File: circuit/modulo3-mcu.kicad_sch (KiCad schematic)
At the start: 24 parts, among them SW1 RST_SW, U1 74LVC2G32DC, U2 AVR64DA64, U3 SN74LVC1G17, U4 UPDI, Y1 32768Hz

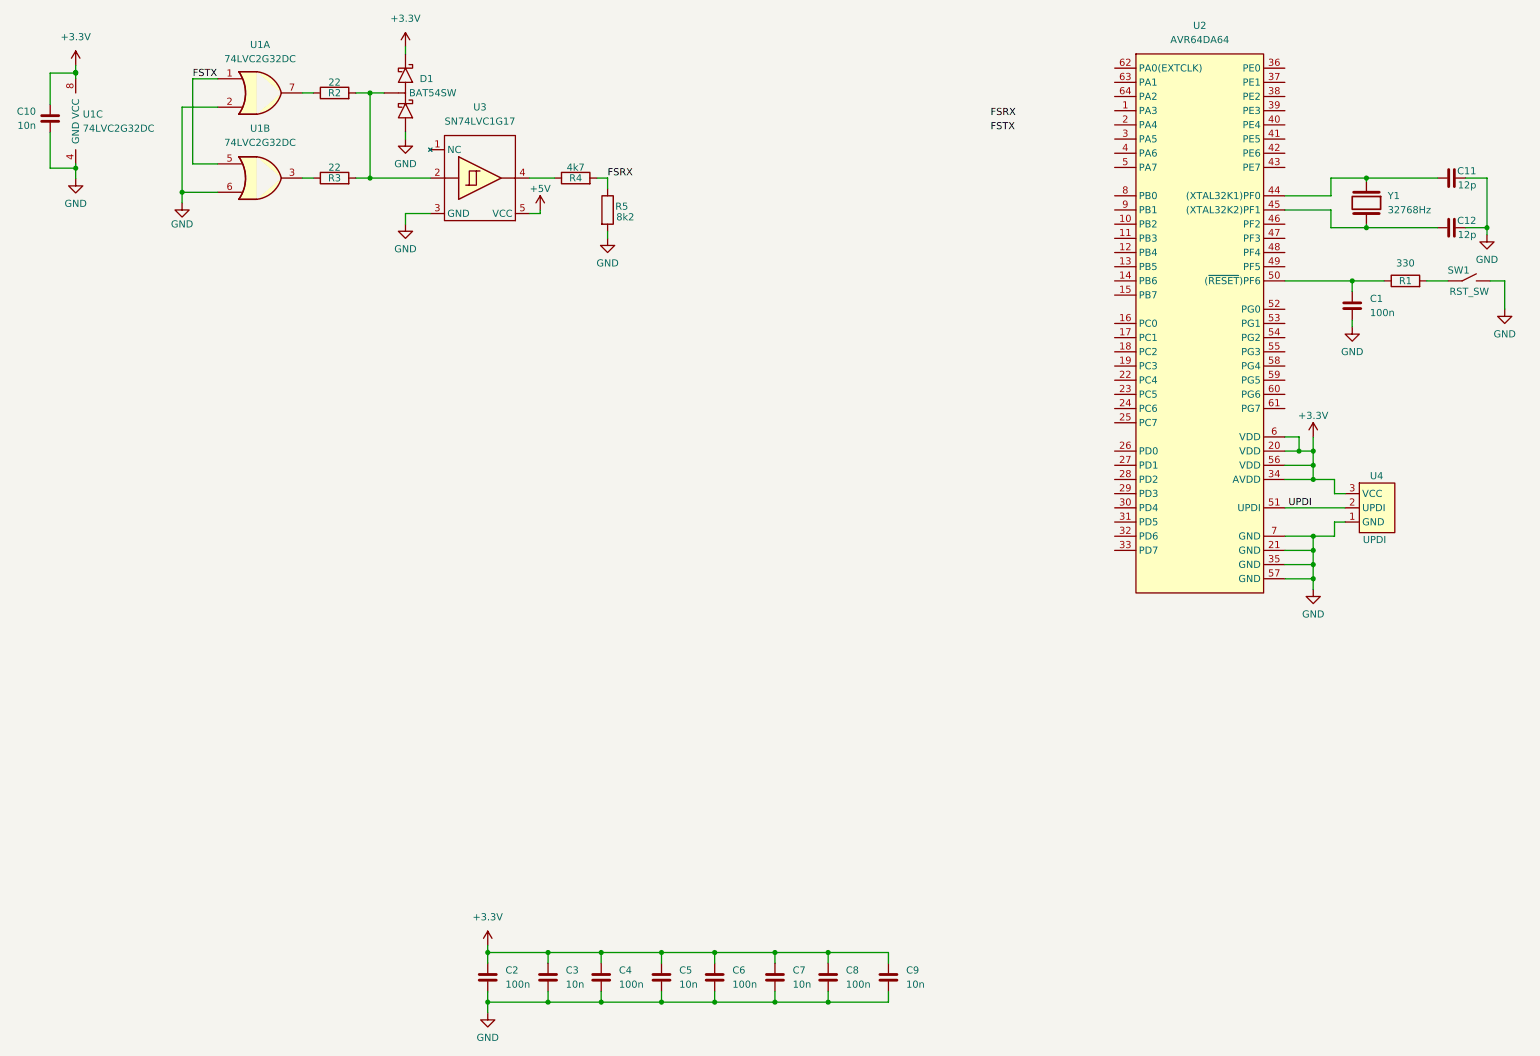
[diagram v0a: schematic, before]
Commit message: mcu board; fv1 board tracing
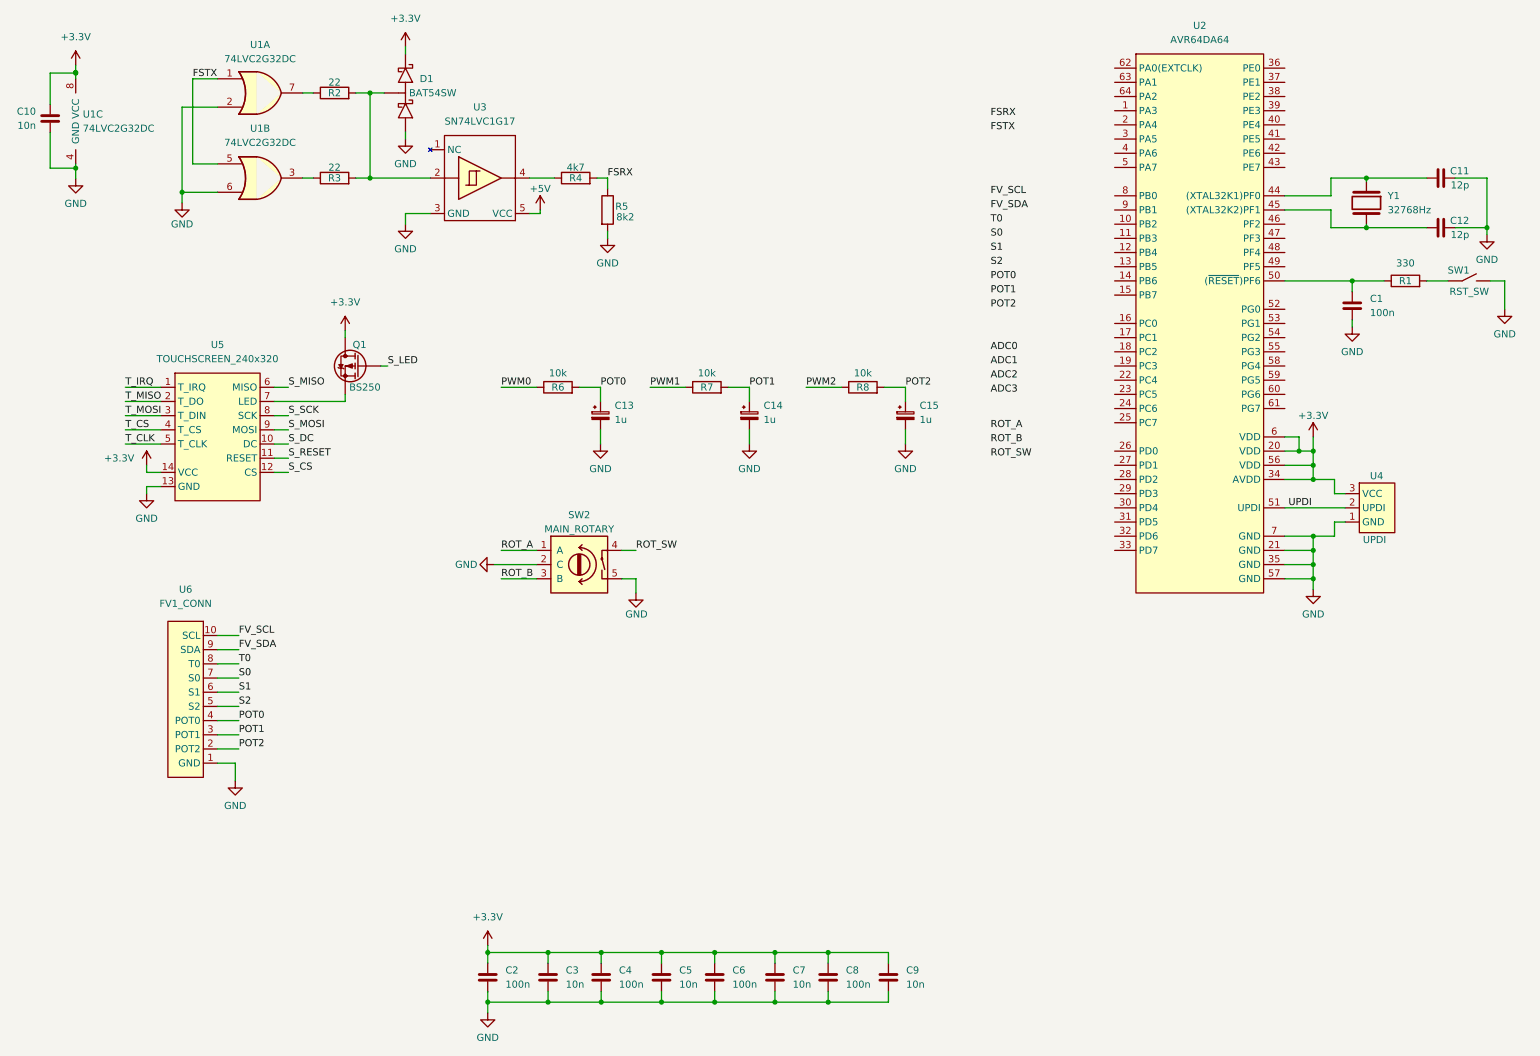
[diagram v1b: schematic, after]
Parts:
- added C13, C14, C15: 1u, symbol myAmp:CPOL
- added Q1: BS250, myAmp:TO-92_Inline_Wide, symbol myAmp:BS250
- added R6, R7, R8: 10k, myAmp:C_1206, symbol myAmp:R
- added SW2: MAIN_ROTARY, symbol myAmp:Rotary_Encoder_Switch
- added U5: TOUCHSCREEN_240x320, symbol myAmp:TOUCHSCREEN_240x320
- added U6: FV1_CONN, symbol myAmp:FV1_CONN
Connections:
- net +3.3V: now also Q1.1 (D), U5.14 (VCC)
- net GND: now also C13.2, C14.2, C15.2, SW2.2 (C), SW2.5, U5.13 (GND), U6.1 (GND)
- new net: Q1.3 (S), U5.7 (LED)
- new net FV_SCL: U6.10 (SCL)
- new net FV_SDA: U6.9 (SDA)
- new net POT0: C13.1, R6.2, U6.4 (POT0)
- new net POT1: C14.1, R7.2, U6.3 (POT1)
- new net POT2: C15.1, R8.2, U6.2 (POT2)
- new net PWM0: R6.1
- new net PWM1: R7.1
- new net PWM2: R8.1
- new net ROT_A: SW2.1 (A)
- new net ROT_B: SW2.3 (B)
- new net ROT_SW: SW2.4
- new net S0: U6.7 (S0)
- new net S1: U6.6 (S1)
- new net S2: U6.5 (S2)
- new net S_CS: U5.12 (CS)
- new net S_DC: U5.10 (DC)
- new net S_LED: Q1.2 (G)
- new net S_MISO: U5.6 (MISO)
- new net S_MOSI: U5.9 (MOSI)
- new net S_RESET: U5.11 (RESET)
- new net S_SCK: U5.8 (SCK)
- new net T0: U6.8 (T0)
- new net T_CLK: U5.5 (T_CLK)
- new net T_CS: U5.4 (T_CS)
- new net T_IRQ: U5.1 (T_IRQ)
- new net T_MISO: U5.2 (T_DO)
- new net T_MOSI: U5.3 (T_DIN)
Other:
- moved on the sheet: C11, C12

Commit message: added touchscreen footprint
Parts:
- added R9: 100, myAmp:C_1206, symbol myAmp:R
- C13, C14, C15: value 1u -> 3u3; footprint (none) -> myAmp:CPOL_D4_P1.5
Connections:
- net T_MISO is gone; now on net S_MISO: U5.2 (T_DO)
- net T_MOSI is gone; now on net S_MOSI: U5.3 (T_DIN)
- net at U5.7 (LED): now also R9.1; no longer Q1.3 (S)
- net T_CLK renamed S_CLK
- new net: Q1.3 (S), R9.2
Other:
- moved on the sheet: U5

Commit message: general layout and board sizes
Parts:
- removed C1: 100n, myAmp:C_1206, symbol myAmp:C
- removed R1: 330, myAmp:C_1206, symbol myAmp:R
- removed SW1: RST_SW, myAmp:Switch_2.5mm, symbol myAmp:SW_SIMPLE
- removed SW2: MAIN_ROTARY, symbol myAmp:Rotary_Encoder_Switch
- added U7: DBG_UART, myAmp:DBG_UART, symbol myAmp:DBG_UART
- R2, R3, R4, R5, R9: footprint myAmp:C_1206 -> myAmp:R_10MM
- R6, R7, R8: footprint myAmp:C_1206 -> myAmp:R_1206
- U5: footprint (none) -> myAmp:TOUCHSCREEN_2.8
- U6: footprint (none) -> myAmp:FV1_CONN
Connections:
- net S_CLK is gone; now on net S_SCK: U5.5 (T_CLK)
- net S_RESET is gone; now on net S_RST: U5.11 (RESET)
- net GND: now also U7.1 (GND)
- net PWM0: now also U2.62 (PA0(EXTCLK))
- net PWM1: now also U2.63 (PA1)
- net PWM2: now also U2.64 (PA2)
- net S_CS: now also U2.10 (PB2)
- net S_DC: now also U2.8 (PB0)
- net S_LED: now also U2.11 (PB3)
- net S_MISO: now also U2.3 (PA5)
- net S_MOSI: now also U2.2 (PA4)
- net S_SCK: now also U2.4 (PA6)
- net T_CS: now also U2.5 (PA7)
- net T_IRQ: now also U2.1 (PA3)
- net DBG_TX: now reaches U2.52 (PG0)
- net DBG_TX: now also U7.2 (TX)
- net S_RST: now reaches U2.9 (PB1)
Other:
- moved on the sheet: C10, C11, C12, U1C, U2, U4, Y1

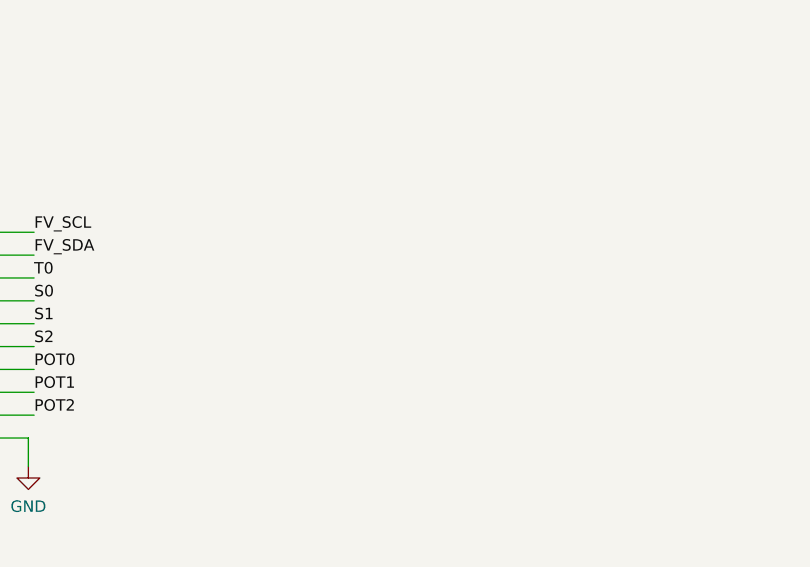
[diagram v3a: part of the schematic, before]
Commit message: added ampctrl and diffaudio; started changing powamp
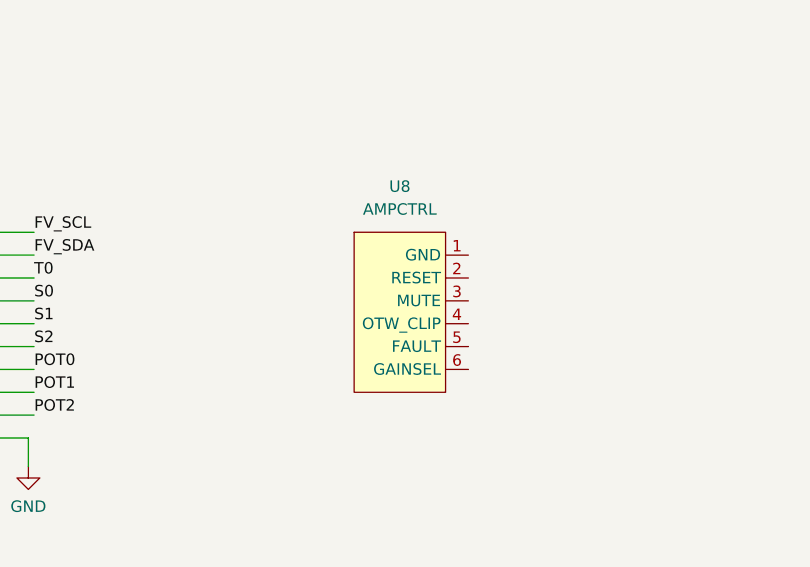
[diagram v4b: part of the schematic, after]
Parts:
- added U8: AMPCTRL, myAmp:AMPCTRL, symbol myAmp:AMPCTRL
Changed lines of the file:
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@@
     (pin "2")
+  )
+  (symbol (lib_id "myAmp:AMPCTRL") (at 95.25 129.54 0) (unit 1)
+    (in_bom yes) (on_board yes) (fields_autoplaced)
+    (property "Reference" "U8" (id 0) (at 93.98 119.38 0))
+    (property "Value" "AMPCTRL" (id 1) (at 93.98 121.92 0))
+    (property "Footprint" "myAmp:AMPCTRL" (id 2) (at 101.6 129.54 0)
+      (effects (font (size 1.27 1.27)) hide)
+    )
+    (property "Datasheet" "" (id 3) (at 101.6 129.54 0))
+    (pin "1")
+    (pin "2")
+    (pin "3")
+    (pin "4")
+    (pin "5")
+    (pin "6")
   )
   (symbol (lib_id "myAmp:C") (at 158.877 185.674 0) (unit 1)
@@
       (reference "U7") (unit 1) (value "DBG_UART") (footprint "myAmp:DBG_UART")
     )
+    (path "/0c7a98ec-78f8-49cd-8480-04f303c2fd21"
+      (reference "U8") (unit 1) (value "AMPCTRL") (footprint "myAmp:AMPCTRL")
+    )
     (path "/54624f9b-2716-4419-b6d6-a5222a4295c4"

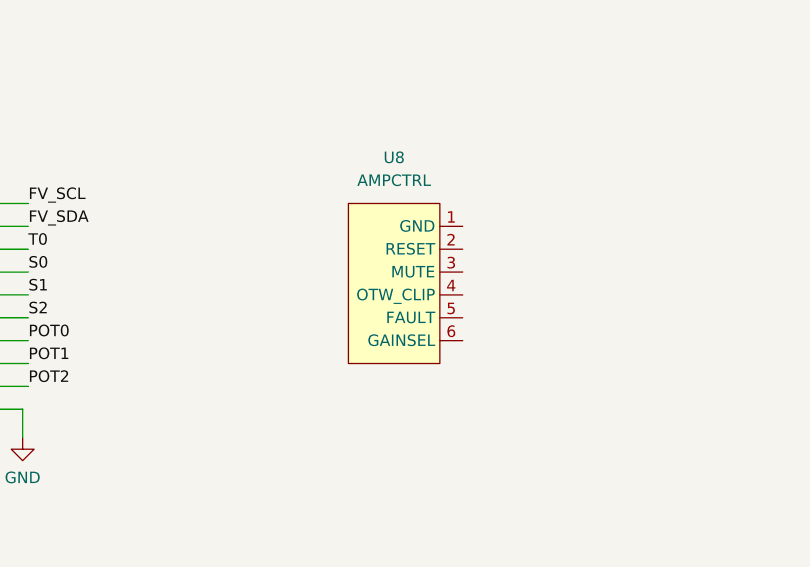
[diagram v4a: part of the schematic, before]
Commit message: got the pcs and holes sizes for mcu, poweamp and fv1
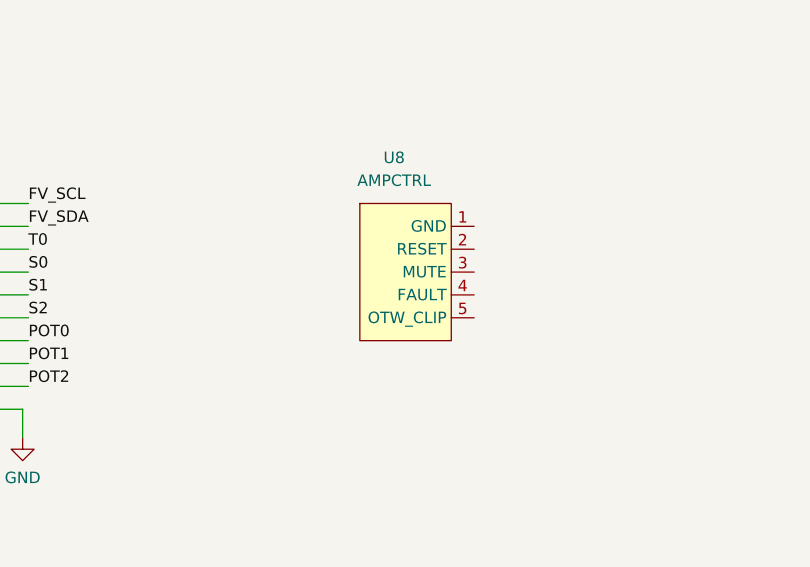
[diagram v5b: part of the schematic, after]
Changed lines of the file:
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@@
     (pin "4")
     (pin "5")
-    (pin "6")
   )
   (symbol (lib_id "myAmp:C") (at 158.877 185.674 0) (unit 1)

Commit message: fv-1 mostly done; power progressed
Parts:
- added U10: PWR_CONN, myAmp:PWR_CONN, symbol myAmp:PWR_CONN
- added U9: ~, myAmp:PREAMP_CONN, symbol myAmp:PREAMP_CONN
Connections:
- net FV_SCL: now also U6.8 (SCL); no longer U6.10 (SCL)
- net FV_SDA: now also U6.7 (SDA); no longer U6.9 (SDA)
- net GND: no longer U6.1 (GND)
- net POT0: now also U6.3 (POT0); no longer U6.4 (POT0)
- net POT1: now also U6.2 (POT1); no longer U6.3 (POT1)
- net POT2: now also U6.1 (POT2); no longer U6.2 (POT2)
- net S0: now also U6.6 (S0); no longer U6.7 (S0)
- net S1: now also U6.5 (S1); no longer U6.6 (S1)
- net S2: now also U6.4 (S2); no longer U6.5 (S2)
- net T0: now also U6.9 (T0); no longer U6.8 (T0)
- new net FV_CLIP: U6.10 (CLP)
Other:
- moved on the sheet: U6

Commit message: lotsa things :)
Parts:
- added C1: 10n, myAmp:C_1206, symbol myAmp:C
- added Q2: BS170, myAmp:TO-92_Inline_Wide, symbol myAmp:NMOS
- added R1, R11, R15: 10k, myAmp:R_10MM, symbol myAmp:R
- added R10: 1k, myAmp:R_10MM, symbol myAmp:R
- added R12, R13, R14: 100, myAmp:R_10MM, symbol myAmp:R
- added U11: FOOTSWITCH, myAmp:FOOTSWITCH, symbol myAmp:FOOTSWITCH
- added U12: ~, myAmp:KNOBS, symbol myAmp:KNOBS
- R6, R7, R8: footprint myAmp:R_1206 -> myAmp:R_10MM
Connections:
- net +3.3V: now also U5.1 (VCC), R11.2, U12.10 (VCC); no longer U4.3 (VCC), U5.14 (VCC)
- net +5V: now also U10.3 (5V)
- net ADC0: now also U12.2 (WIPE1)
- net ADC1: now also U12.3 (WIPE2)
- net ADC2: now also U12.4 (WIPE3)
- net ADC3: now also U12.5 (WIPE4)
- net DBG_TX: no longer U2.52 (PG0)
- net FV_SCL: now also U2.47 (PF3)
- net FV_SDA: now also U2.46 (PF2)
- net GND: now also U10.1 (GND), U5.2 (GND), U8.1 (GND), U9.3 (GND), C1.2, Q2.3 (S), R10.2, R15.1, U11.1 (SLEEVE), U12.1 (GND); no longer U5.13 (GND)
- net PWM0: now also U2.52 (PG0); no longer U2.62 (PA0(EXTCLK))
- net PWM1: now also U2.53 (PG1); no longer U2.63 (PA1)
- net PWM2: now also U2.54 (PG2); no longer U2.64 (PA2)
- net S0: now also U2.48 (PF4)
- net S1: now also U2.49 (PF5)
- net S2: now also U2.50 ((~{RESET})PF6)
- net S_CS: now also U5.3 (CS); no longer U2.10 (PB2), U5.12 (CS)
- net S_DC: now also U5.5 (DC); no longer U2.8 (PB0), U5.10 (DC)
- net S_LED: no longer U2.11 (PB3)
- net S_MISO: now also U2.13 (PB5), U5.13 (T_DO), U5.9 (MISO); no longer U2.3 (PA5), U5.2 (T_DO), U5.6 (MISO)
- net S_MOSI: now also U2.12 (PB4), U5.12 (T_DIN), U5.6 (MOSI); no longer U2.2 (PA4), U5.3 (T_DIN), U5.9 (MOSI)
- net S_RST: now also U5.4 (RESET); no longer U2.9 (PB1), U5.11 (RESET)
- net S_SCK: now also U2.14 (PB6), U5.10 (T_CLK), U5.7 (SCK); no longer U2.4 (PA6), U5.5 (T_CLK), U5.8 (SCK)
- net T_CS: now also U5.11 (T_CS); no longer U2.5 (PA7), U5.4 (T_CS)
- net T_IRQ: now also U2.15 (PB7), U5.14 (T_IRQ); no longer U2.1 (PA3), U5.1 (T_IRQ)
- net at U8.2 (RESET): now also R12.1, R15.2
- net MUTE: now reaches U8.3 (MUTE)
- net MUTE: now also Q2.1 (D)
- net at U8.4 (FAULT): now also R14.1
- net at U8.5 (OTW_CLIP): now also R13.1
- net MIX_SDA: now reaches U9.1 (SDA)
- net MIX_SDA: now also U2.18 (PC2)
- net MIX_SCL: now reaches U9.2 (SCL)
- net MIX_SCL: now also U2.19 (PC3)
- net at R9.1: now also U5.8 (LED); no longer U5.7 (LED)
- net at D1.3, R2.2, R3.2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: now also U11.2 (TIP)
- net OTW_CLIP: now reaches U2.58 (PG4)
- net OTW_CLIP: now also R13.2
- net FAULT: now reaches U2.59 (PG5)
- net FAULT: now also R14.2
- net POW_RESET: now reaches U2.60 (PG6)
- net POW_RESET: now also R12.2
- net at U10.2 (30V): now also R1.1
- new net IN_V: C1.1, R1.2, R10.1
- new net MUTE_CTRL: Q2.2 (G), R11.1
- new net RE_A: U12.6 (RE_A)
- new net RE_B: U12.7 (RE_B)
- new net RE_SW: U12.8 (RE_SW)
- no-connect marks 0 -> 4
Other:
- moved on the sheet: C11, C12, D1, R2, R3, R4, R5, U1A, U1B, U3, U7, U8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

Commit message: routing mcu
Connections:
- net +3.3V: now also C10.1, U1.8 (VCC)
- net FAULT: now also U2.62 (PA0(EXTCLK)); no longer U2.59 (PG5)
- net MUTE_CTRL: now also U2.64 (PA2)
- net OTW_CLIP: now also U2.61 (PG7); no longer U2.58 (PG4)
- net S_CS: now also U2.8 (PB0)
- net S_DC: now also U2.10 (PB2)
- net S_LED: now also U2.5 (PA7)
- net S_RST: now also U2.9 (PB1)
- net T_CS: now also U2.11 (PB3)
- net PA_RESET: now reaches U2.63 (PA1)
- net PA_RESET: now also R12.2
- net POW_RESET: no longer names the net of U2.60 (PG6)
- net POW_RESET: no longer R12.2
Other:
- moved on the sheet: C10, U1C
